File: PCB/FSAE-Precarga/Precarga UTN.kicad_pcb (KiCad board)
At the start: 2 copper layers, 2 parts, among them U1 ZC323000

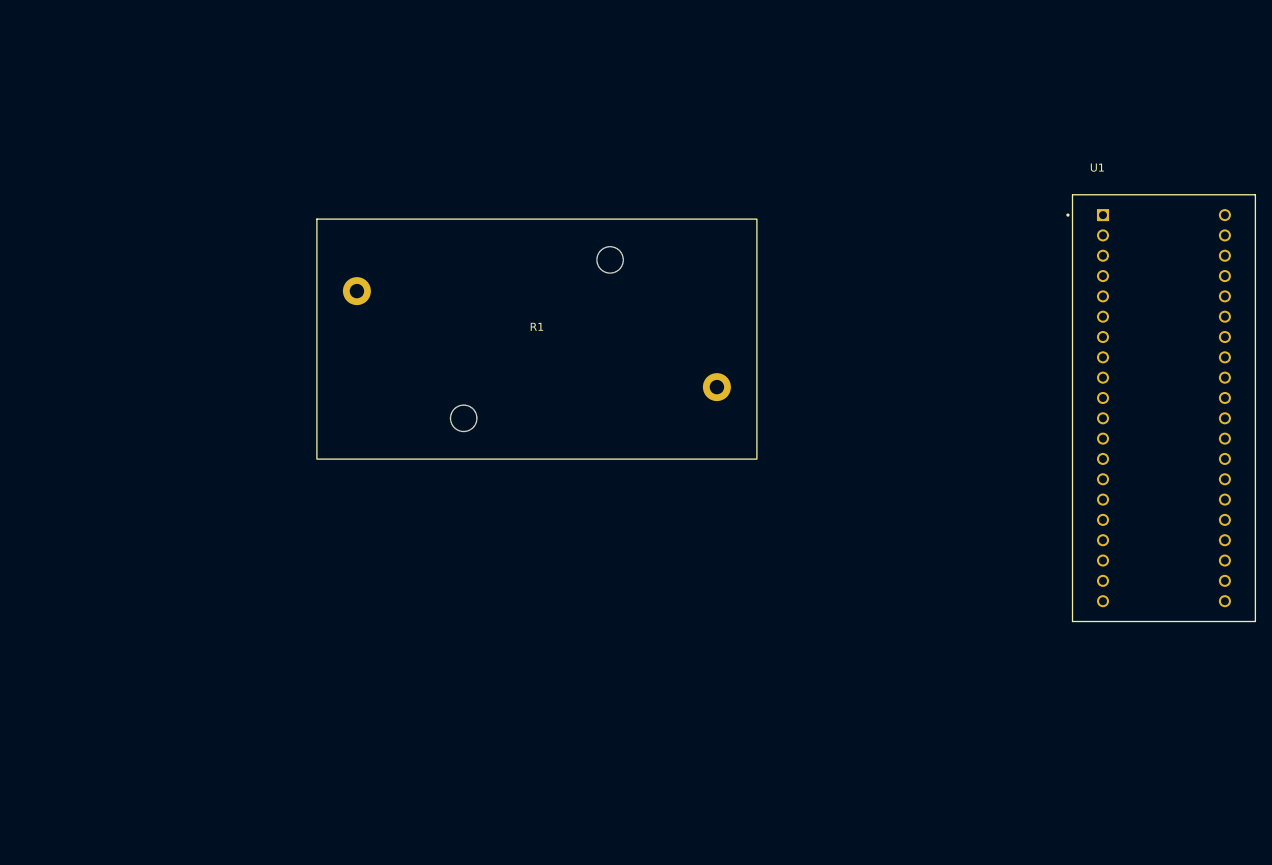
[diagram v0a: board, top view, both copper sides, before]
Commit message: Version avanzada (NO final) de la placa de precarga
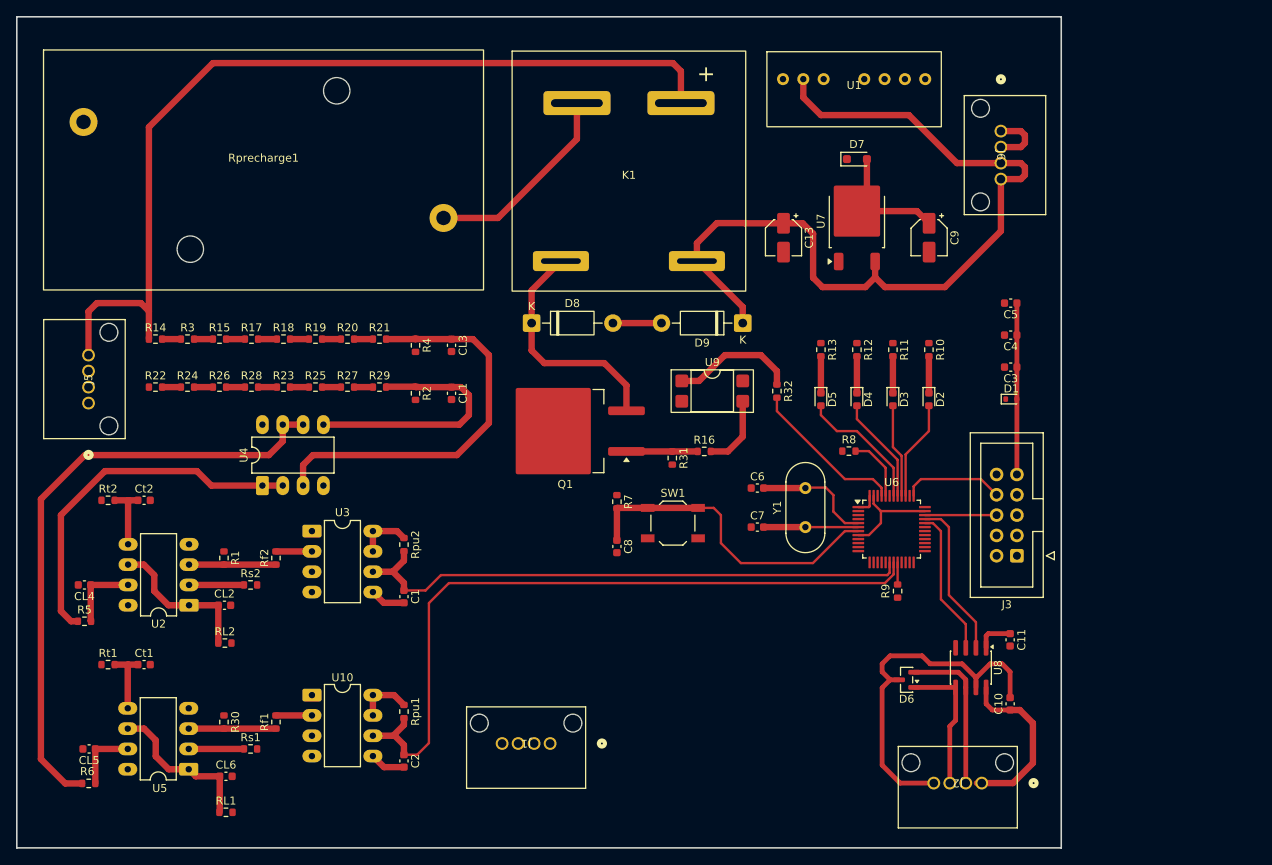
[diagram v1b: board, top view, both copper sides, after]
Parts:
- added C1: 10p, Capacitor_SMD:C_0603_1608Metric, F.Cu at (126.9, 117.7)
- added C10: 100n, Capacitor_SMD:C_0603_1608Metric, F.Cu at (202.7, 131.1)
- added C11: 100n, Capacitor_SMD:C_0603_1608Metric, F.Cu at (202.7, 123.1)
- added C13: 10u, Capacitor_SMD:CP_Elec_4x5.4, F.Cu at (174.3, 72.8)
- added C2: 10p, Capacitor_SMD:C_0603_1608Metric, F.Cu at (126.9, 138.2)
- added C3: 100n, Capacitor_SMD:C_0603_1608Metric, F.Cu at (202.7, 89.0)
- added C4: 100n, Capacitor_SMD:C_0603_1608Metric, F.Cu at (202.7, 85.0)
- added C5: 100n, Capacitor_SMD:C_0603_1608Metric, F.Cu at (202.7, 81.0)
- added C6: 20p, Capacitor_SMD:C_0603_1608Metric, F.Cu at (171.1, 104.1)
- added C7: 20p, Capacitor_SMD:C_0603_1608Metric, F.Cu at (171.1, 109.0)
- added C8: 100n, Capacitor_SMD:C_0603_1608Metric, F.Cu at (153.5, 111.4)
- added C9: 10u, Capacitor_SMD:CP_Elec_4x5.4, F.Cu at (192.5, 72.8)
- added CL1: 10n, Capacitor_SMD:C_0603_1608Metric, F.Cu at (132.8, 92.3)
- added CL2: 10n, Capacitor_SMD:C_0603_1608Metric, F.Cu at (104.4, 118.8)
- added CL3: 10n, Capacitor_SMD:C_0603_1608Metric, F.Cu at (132.8, 86.3)
- added CL4: 10n, Capacitor_SMD:C_0603_1608Metric, F.Cu at (86.9, 116.2)
- added CL5: 10n, Capacitor_SMD:C_0603_1608Metric, F.Cu at (87.5, 136.7)
- added CL6: 10n, Capacitor_SMD:C_0603_1608Metric, F.Cu at (104.6, 140.2)
- added Ct1: 4.7n, Capacitor_SMD:C_0603_1608Metric, F.Cu at (94.4, 126.2)
- added Ct2: 4.7n, Capacitor_SMD:C_0603_1608Metric, F.Cu at (94.4, 105.7)
- added D1: BSD5C031V, Diode_SMD:D_SOD-523, F.Cu at (202.8, 93.0)
- added D2: LED_Verde, LED_SMD:LED_0603_1608Metric, F.Cu at (192.5, 93.0)
- added D3: LED_Amarillo, LED_SMD:LED_0603_1608Metric, F.Cu at (188.0, 93.0)
- added D4: LED_Verde, LED_SMD:LED_0603_1608Metric, F.Cu at (183.5, 93.0)
- added D5: LED_Rojo, LED_SMD:LED_0603_1608Metric, F.Cu at (179.0, 93.0)
- added D6: NUP2105L, Package_TO_SOT_SMD:SOT-23, F.Cu at (189.7, 128.1)
- added D7: 1N4148W, Diode_SMD:D_SOD-323_HandSoldering, F.Cu at (183.5, 63.0)
- added D8: 1N5363, Diode_THT:D_DO-41_SOD81_P10.16mm_Horizontal, F.Cu at (142.8, 83.5)
- added D9: SB5100, Diode_THT:D_DO-41_SOD81_P10.16mm_Horizontal, F.Cu at (169.2, 83.5)
- added J1: Conn_01x04, GeneratedConnector:Molex_Mini50, F.Cu at (145.1, 136.1)
- added J2: Conn_01x04, GeneratedConnector:Molex_Mini50, F.Cu at (199.1, 141.0)
- added J3: Programming Port, Connector_IDC:IDC-Header_2x05_P2.54mm_Vertical, F.Cu at (203.5, 112.6)
- added J5: Conn_01x04, GeneratedConnector:Molex_Mini50, F.Cu at (87.5, 93.5)
- added J6: Conn_01x04, GeneratedConnector:Molex_Mini50, F.Cu at (201.5, 59.5)
- added K1: RER02, Mis_Huellas:RER02PAX, F.Cu at (155.0, 64.5)
- added Q1: IRF640S, Package_TO_SOT_SMD:TO-263-2, F.Cu at (147.0, 97.0)
- added R1: 10k, Resistor_SMD:R_0603_1608Metric, F.Cu at (104.4, 112.9)
- added R10: 220, Resistor_SMD:R_0603_1608Metric, F.Cu at (192.5, 86.8)
- added R11: 220, Resistor_SMD:R_0603_1608Metric, F.Cu at (188.0, 86.8)
- added R12: 220, Resistor_SMD:R_0603_1608Metric, F.Cu at (183.5, 86.8)
- added R13: 220, Resistor_SMD:R_0603_1608Metric, F.Cu at (179.0, 86.8)
- added R14: 49.9k, Resistor_SMD:R_0603_1608Metric, F.Cu at (95.8, 85.5)
- added R15: 49.9k, Resistor_SMD:R_0603_1608Metric, F.Cu at (103.8, 85.5)
- added R16: 1k, Resistor_SMD:R_0603_1608Metric, F.Cu at (164.4, 99.5)
- added R17: 49.9k, Resistor_SMD:R_0603_1608Metric, F.Cu at (107.8, 85.5)
- added R18: 49.9k, Resistor_SMD:R_0603_1608Metric, F.Cu at (111.8, 85.5)
- added R19: 49.9k, Resistor_SMD:R_0603_1608Metric, F.Cu at (115.8, 85.5)
- added R2: 5k, Resistor_SMD:R_0603_1608Metric, F.Cu at (128.3, 92.3)
- added R20: 49.9k, Resistor_SMD:R_0603_1608Metric, F.Cu at (119.8, 85.5)
- added R21: 49.9k, Resistor_SMD:R_0603_1608Metric, F.Cu at (123.8, 85.5)
- added R22: 49.9k, Resistor_SMD:R_0603_1608Metric, F.Cu at (95.8, 91.5)
- added R23: 49.9k, Resistor_SMD:R_0603_1608Metric, F.Cu at (111.8, 91.5)
- added R24: 49.9k, Resistor_SMD:R_0603_1608Metric, F.Cu at (99.8, 91.5)
- added R25: 49.9k, Resistor_SMD:R_0603_1608Metric, F.Cu at (115.8, 91.5)
- added R26: 49.9k, Resistor_SMD:R_0603_1608Metric, F.Cu at (103.8, 91.5)
- added R27: 49.9k, Resistor_SMD:R_0603_1608Metric, F.Cu at (119.8, 91.5)
- added R28: 49.9k, Resistor_SMD:R_0603_1608Metric, F.Cu at (107.8, 91.5)
- added R29: 49.9k, Resistor_SMD:R_0603_1608Metric, F.Cu at (123.8, 91.5)
- added R3: 49.9k, Resistor_SMD:R_0603_1608Metric, F.Cu at (99.8, 85.5)
- added R30: 10k, Resistor_SMD:R_0603_1608Metric, F.Cu at (104.4, 133.4)
- added R31: 100k, Resistor_SMD:R_0603_1608Metric, F.Cu at (160.4, 100.4)
- added R32: 1k, Resistor_SMD:R_0603_1608Metric, F.Cu at (173.5, 92.0)
- added R4: 5k, Resistor_SMD:R_0603_1608Metric, F.Cu at (128.3, 86.3)
- added R5: 10k, Resistor_SMD:R_0603_1608Metric, F.Cu at (86.9, 120.8)
- added R6: 10k, Resistor_SMD:R_0603_1608Metric, F.Cu at (87.5, 141.0)
- added R7: 10k, Resistor_SMD:R_0603_1608Metric, F.Cu at (153.5, 105.8)
- added R8: 10k, Resistor_SMD:R_0603_1608Metric, F.Cu at (182.5, 99.5)
- added R9: 10k, Resistor_SMD:R_0603_1608Metric, F.Cu at (188.6, 117.0)
- added RL1: 10k, Resistor_SMD:R_0603_1608Metric, F.Cu at (104.6, 144.7)
- added RL2: 10k, Resistor_SMD:R_0603_1608Metric, F.Cu at (104.5, 123.5)
- added Rf1: 2.2k, Resistor_SMD:R_0603_1608Metric, F.Cu at (110.9, 133.4)
- added Rf2: 2.2k, Resistor_SMD:R_0603_1608Metric, F.Cu at (110.9, 112.9)
- added Rpu1: 1k, Resistor_SMD:R_0603_1608Metric, F.Cu at (126.9, 132.1)
- added Rpu2: 1k, Resistor_SMD:R_0603_1608Metric, F.Cu at (126.9, 111.2)
- added Rs1: 10k, Resistor_SMD:R_0603_1608Metric, F.Cu at (107.7, 136.7)
- added Rs2: 10k, Resistor_SMD:R_0603_1608Metric, F.Cu at (107.7, 116.2)
- added Rt1: 6.8k, Resistor_SMD:R_0603_1608Metric, F.Cu at (89.9, 126.2)
- added Rt2: 6.8k, Resistor_SMD:R_0603_1608Metric, F.Cu at (89.9, 105.7)
- added SW1: SW_MEC_5E, Button_Switch_SMD:SW_SPST_TL3342, F.Cu at (160.5, 108.5)
- added U10: 6N137, Package_DIP:DIP-8_W7.62mm_LongPads, F.Cu at (115.4, 130.0)
- added U2: LM331N, Package_DIP:DIP-8_W7.62mm_LongPads, F.Cu at (100.0, 118.8)
- added U3: 6N137, Package_DIP:DIP-8_W7.62mm_LongPads, F.Cu at (115.4, 109.5)
- added U4: LM2904, Package_DIP:DIP-8_W7.62mm_LongPads, F.Cu at (109.2, 103.8)
- added U5: LM331N, Package_DIP:DIP-8_W7.62mm_LongPads, F.Cu at (100.0, 139.3)
- added U6: STM32F103C8Tx, Package_QFP:LQFP-48_7x7mm_P0.5mm, F.Cu at (187.8, 109.2)
- added U7: LM1117DT-3.3, Package_TO_SOT_SMD:TO-252-2, F.Cu at (183.5, 70.8)
- added U8: ISO1044BD, Package_SO:SOIC-8_3.9x4.9mm_P1.27mm, F.Cu at (197.7, 126.6)
- added U9: PC817, Package_DIP:DIP-4_W7.62mm_SMDSocket_SmallPads, F.Cu at (165.4, 92.0)
- added Y1: Crystal, Crystal:Crystal_HC49-4H_Vertical, F.Cu at (177.1, 109.0)
- Rprecharge1: renamed from R1; value R -> 470
- U1: value ZC323000 -> SPAN02E-12; footprint MODULE_ZC323000.preety:MODULE_ZC323000 -> Mis_Huellas:SPAN02E-12
- moved U1 55.6 mm to (183.2, 54.3)
- moved Rprecharge1 40.2 mm to (86.8, 64.4)
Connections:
- Rprecharge1 pad 1: unconnected-(R1-Pad1) -> /VRprec-
- Rprecharge1 pad 2: unconnected-(R1-Pad2) -> Net-(K1-PadA2-)
- U1 pad 1: unconnected-(U1-VB-Pad1) -> Gnd_GLV
- U1 pad 2: unconnected-(U1-C13-Pad2) -> 12V_GLV
- U1 pad 6: unconnected-(U1-A1-Pad6) -> 12V_TS
- U1 pad 7: unconnected-(U1-A2-Pad7) -> Gnd_TS
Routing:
- net /VRprec+: track 0.00 -> 114.6 mm
- net 12V_GLV: track 0.00 -> 108.1 mm
- net LogicSigPrec-: track 0.00 -> 90.6 mm
- net Net-(U4B--): track 0.00 -> 76.8 mm
- net LogicSigPrec+: track 0.00 -> 71.5 mm
- net 3.3V_GLV: track 0.00 -> 63.6 mm
- net Net-(U4A-+): track 0.00 -> 50.2 mm
- net Net-(U4A--): track 0.00 -> 45.4 mm
- net /CAN/Gnd2: track 0.00 -> 44.5 mm
- net RESET_uC: track 0.00 -> 40.8 mm
- net Net-(U4B-+): track 0.00 -> 32.0 mm
- net Net-(D8-K): track 0.00 -> 29.5 mm
- net Gnd_GLV: track 0.00 -> 29.0 mm
- net Net-(K1-PadA2-): track 0.00 -> 25.3 mm
- net /CAN/Vcc2: track 0.00 -> 21.9 mm
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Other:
- board outline added: 130.6 x 103.9 mm

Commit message: Version avanzada de la placa de Precarga
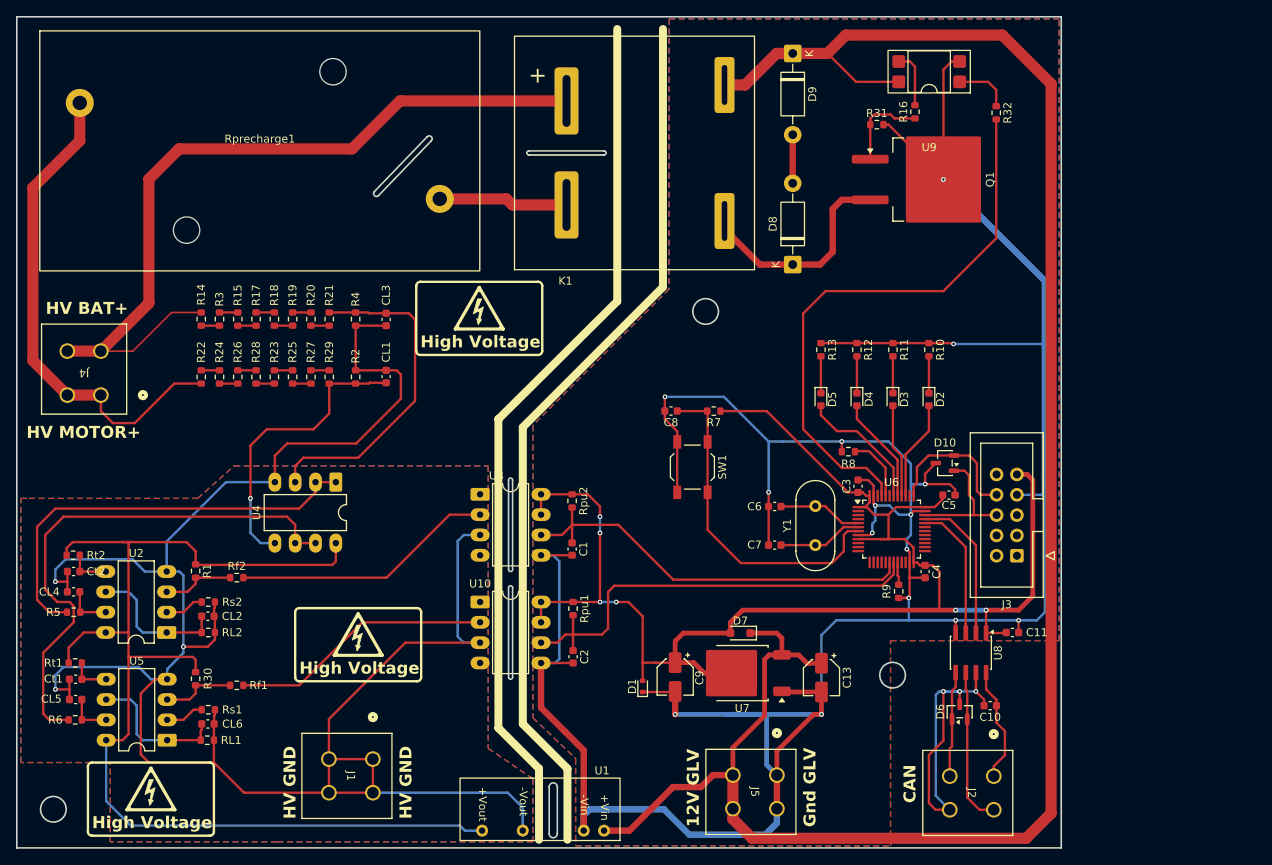
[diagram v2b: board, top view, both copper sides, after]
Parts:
- removed J6: Conn_01x04, GeneratedConnector:Molex_Mini50
- added D10: ESDA5V3L, Package_TO_SOT_SMD:SOT-23-3, F.Cu at (194.5, 101.0)
- added J4: 39310040, footprints:CONN_SD-5566-002_04_MOL, F.Cu at (89.0, 92.5)
- added REF**: Symbol_HighVoltage_Triangle_6x6mm_Copper, Symbol:Symbol_HighVoltage_Triangle_6x6mm_Copper, F.Cu at (95.2, 141.7)
- added REF**: Symbol_HighVoltage_Triangle_6x6mm_Copper, Symbol:Symbol_HighVoltage_Triangle_6x6mm_Copper, F.Cu at (121.2, 122.4)
- added REF**: Symbol_HighVoltage_Triangle_6x6mm_Copper, Symbol:Symbol_HighVoltage_Triangle_6x6mm_Copper, F.Cu at (136.3, 81.6)
- J1, J2, J5: value Conn_01x04 -> 39310040; footprint GeneratedConnector:Molex_Mini50 -> footprints:CONN_SD-5566-002_04_MOL
- U1: value SPAN02E-12 -> NMK0512SAC; footprint Mis_Huellas:SPAN02E-12 -> Mis_Huellas:NMK0512SAC
- moved U1 98.2 mm to (143.9, 144.3), turned to 180 degrees
- moved J5 97.8 mm to (173.5, 140.0), turned to -90 degrees
- moved C9 63.4 mm to (160.8, 127.7)
- moved D7 61.0 mm to (168.9, 122.2), turned to 180 degrees
- moved D1 58.4 mm to (156.7, 128.9), turned to 90 degrees
- moved U7 58.3 mm to (169.1, 127.3), turned to 180 degrees
- moved Q1 55.5 mm to (192.8, 65.6), turned to 0 degrees
- moved C13 55.2 mm to (179.1, 127.8)
- moved R16 50.0 mm to (190.8, 57.1), turned to 90 degrees
- moved R31 48.9 mm to (186.0, 58.7), turned to 0 degrees
- moved U9 48.3 mm to (192.5, 52.1), turned to 180 degrees
- moved R32 44.3 mm to (200.9, 57.2)
- moved D9 34.3 mm to (175.5, 49.8), turned to -90 degrees
- moved D8 33.4 mm to (175.5, 76.2), turned to 90 degrees
- moved C4 31.4 mm to (192.0, 114.6), turned to -90 degrees
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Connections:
- J5 pad 1: /VRprec- -> Gnd_GLV
- J5 pad 2: /VRprec- -> Gnd_GLV
- J5 pad 3: /VRprec+ -> 12V_GLV
- J5 pad 4: /VRprec+ -> 12V_GLV
- U1 pad 1: Gnd_GLV -> 12V_GLV
- U1 pad 2: 12V_GLV -> Gnd_GLV
- U1 pad 7: Gnd_TS -> 12V_TS
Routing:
- net Gnd_GLV: track 29.0 -> 413.6 mm, vias 0 -> 15
- net Gnd_TS: track 0.00 -> 259.8 mm, vias 0 -> 3
- net 12V_TS: track 0.00 -> 143.9 mm
- net 12V_GLV: track 108.1 -> 244.1 mm
- net 3.3V_GLV: track 63.6 -> 189.6 mm, vias 0 -> 6
- net /VRprec-: track 0.00 -> 62.8 mm
- net PCH: track 19.7 -> 71.5 mm
- net LogicSigPrec-: track 90.6 -> 56.2 mm
- net Net-(U3-A): track 4.50 -> 32.9 mm
- net Net-(U10-A): track 4.50 -> 32.9 mm
- net LogicSigPrec+: track 71.5 -> 53.0 mm
- net /VRprec+: track 114.6 -> 99.3 mm
- net Net-(U4B--): track 76.8 -> 67.2 mm
- net Net-(K1-PadA2-): track 25.3 -> 16.2 mm
- net Net-(R32-Pad1): track 15.7 -> 7.02 mm
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- added copper zone on B.Cu, net Gnd_GLV
- added copper zone on F.Cu, net Gnd_GLV
- added copper zone on B.Cu, net Gnd_TS
- added copper zone on F.Cu, net Gnd_TS
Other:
- outline, holes or cut-outs redrawn
- board text added: "12V GLV"
- board text added: "CAN"
- board text added: "Gnd GLV"
- board text added: "HV BAT+"
- board text added: "HV GND"
- board text added: "HV MOTOR+"
- board text added: "High Voltage"
